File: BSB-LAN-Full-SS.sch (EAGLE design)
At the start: 120 parts, among them IC1 LAN8710A-EZC, IC2 TPS2376DDA, IC3 TX4138, IC4 SY8089AAAC, IC6 CH340X, Q1 BC847, Q2 BC857, Q3 BC847, Q4 WPM2015-3/TR, Q5 BC847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

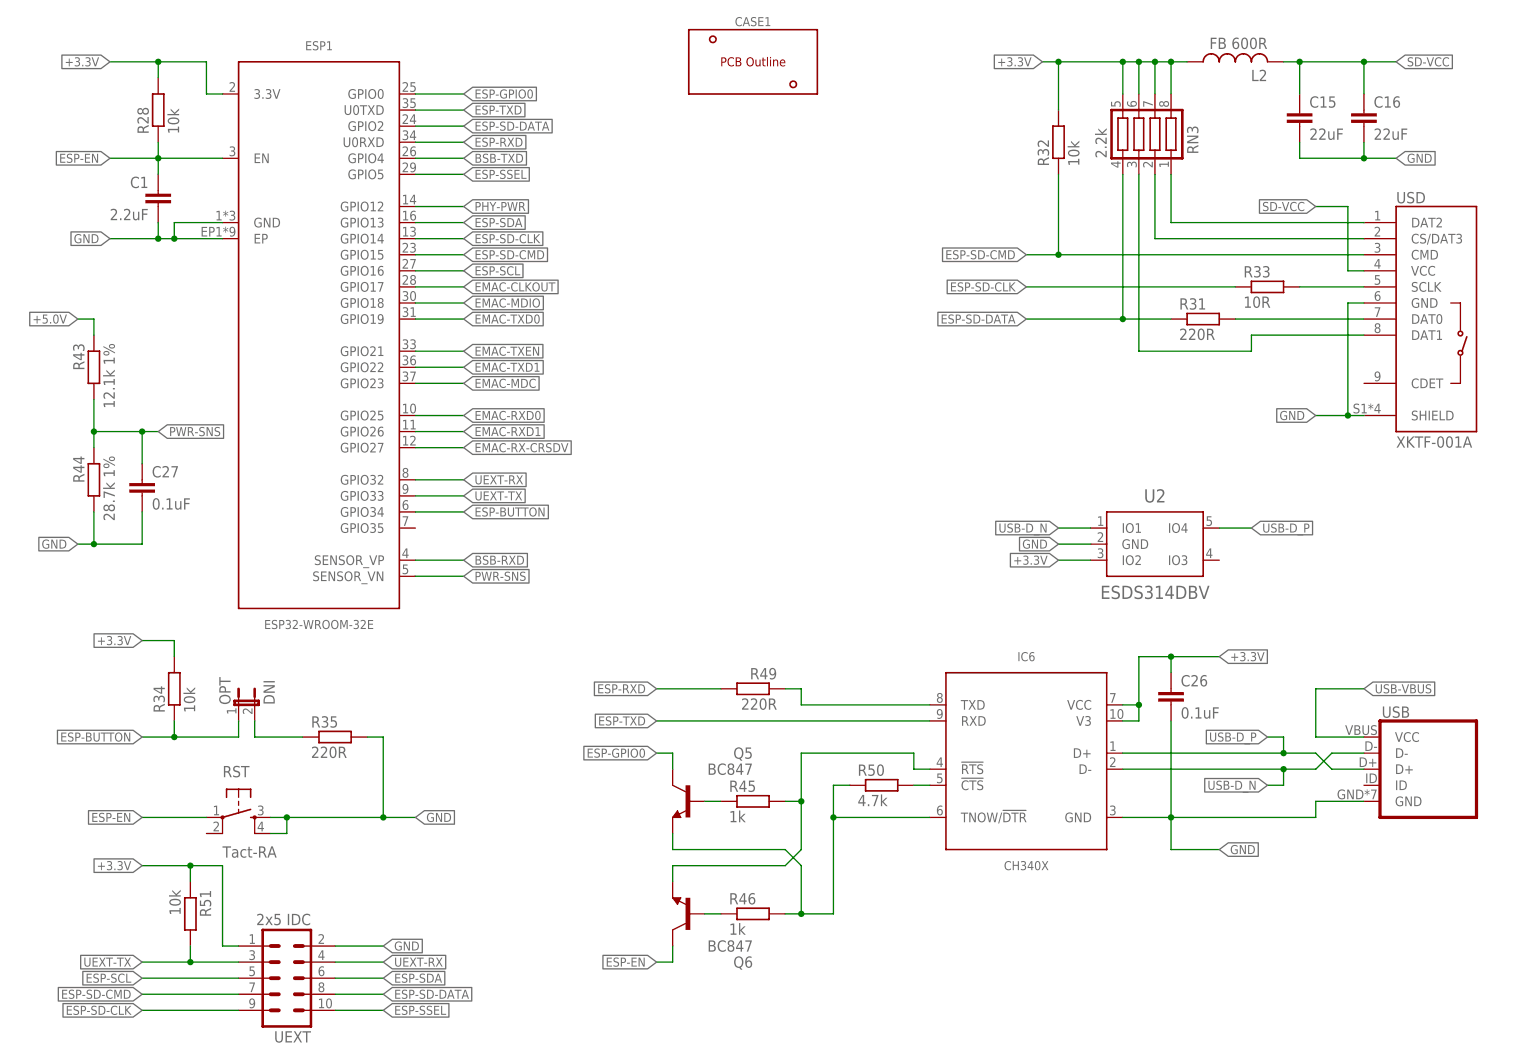
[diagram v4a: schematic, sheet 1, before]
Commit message: Add Missing Pull-Up Resistors on I2C
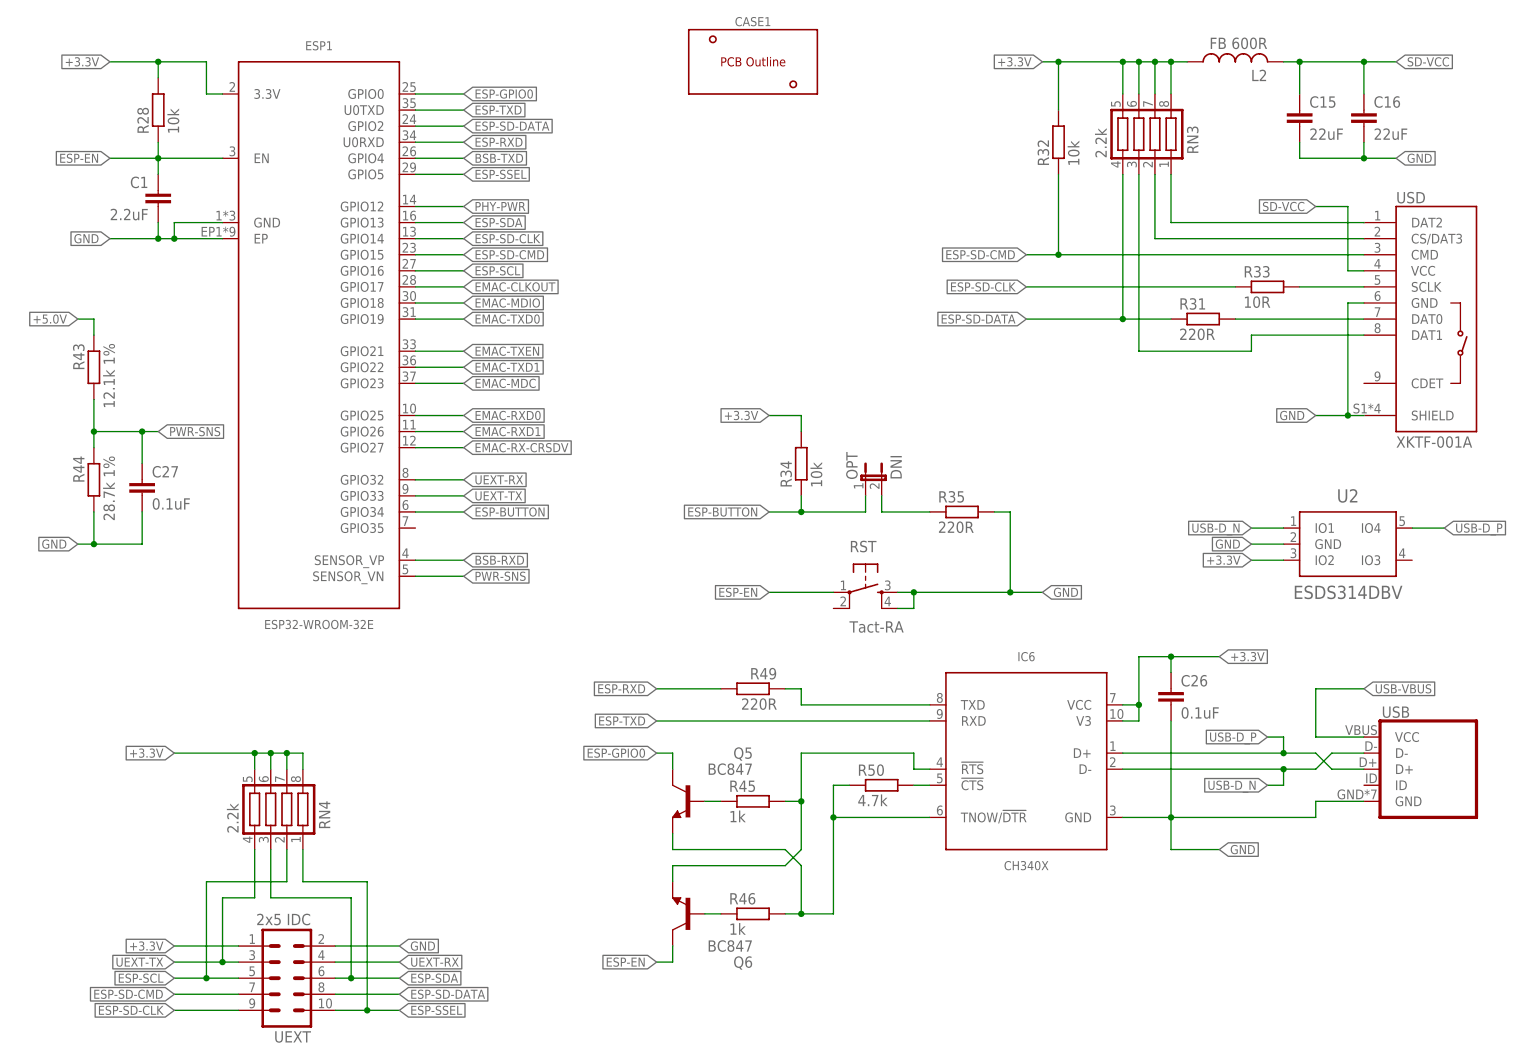
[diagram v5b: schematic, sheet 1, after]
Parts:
- removed R51: 10k, BSB-LAN:R-EU_R0402
- added RN4: 2.2k, BSB-LAN:R-NET-04-R1206
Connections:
- net +3.3V: now also RN4.5, RN4.6, RN4.7, RN4.8; no longer R51.1
- net ESP-SCL: now also RN4.2
- net ESP-SDA: now also RN4.3
- net ESP-SSEL: now also RN4.1
- net UEXT-TX: now also RN4.4; no longer R51.2
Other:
- moved on the sheet: OPT, R34, R35, RST, U2

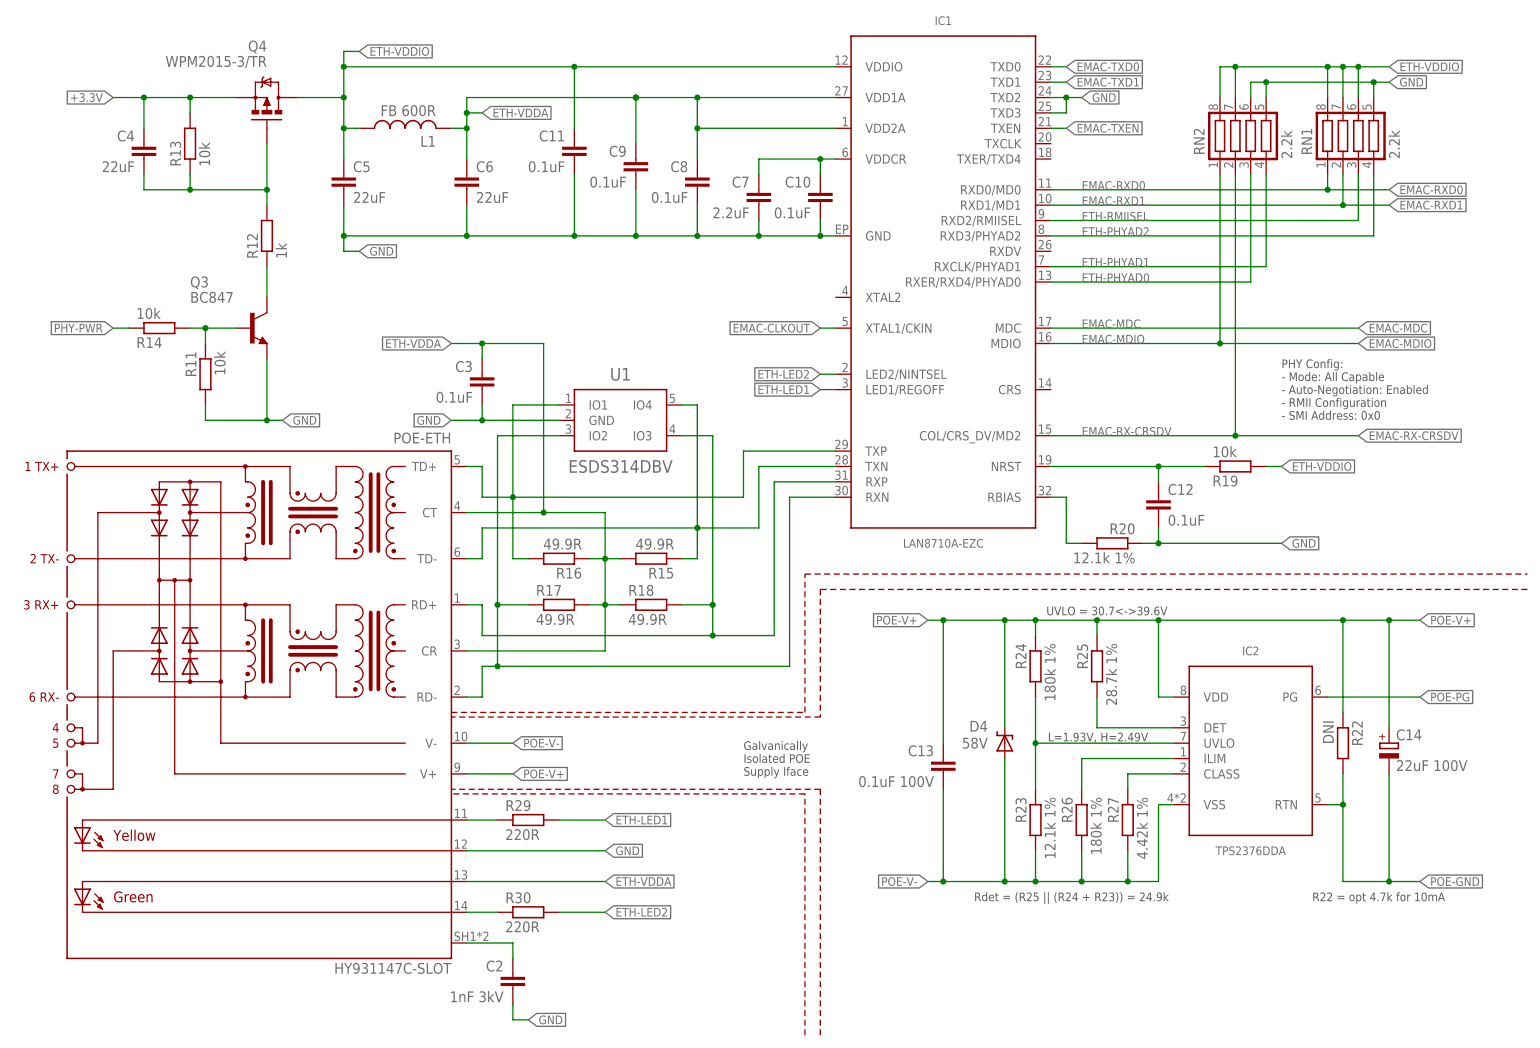
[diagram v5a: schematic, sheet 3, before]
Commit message: Correct Pinout of DC-DC Converter
Not sure quite how I messed up the pin assignments that badly!
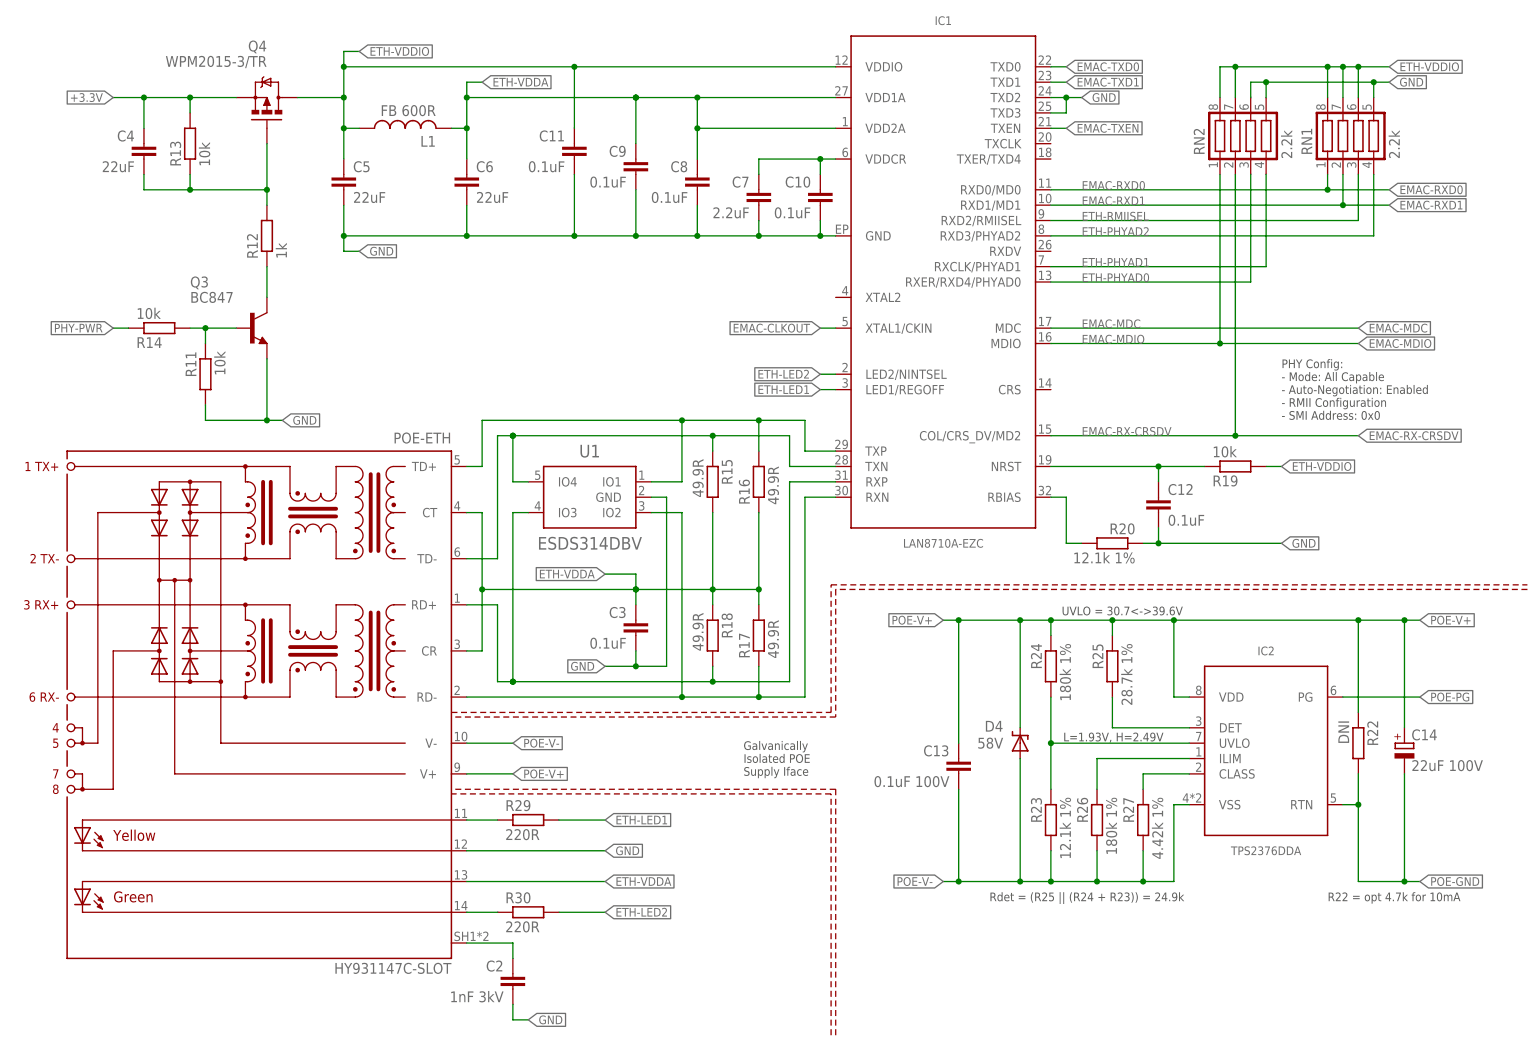
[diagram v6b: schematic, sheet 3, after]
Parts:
- R43: value 12.1k 1% -> 180k 1%
- R44: value 28.7k 1% -> 330k; device BSB-LAN:R-EU_R0402 -> BSB-LAN:R-EU_R0603L
- RST: value Tact-RA -> Tact 19mm
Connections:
- removed net POE-DC-POK-NC: IC3.POK
- net UEXT-RX: now also RN4.4
- net UEXT-TX: no longer RN4.4
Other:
- moved on the sheet: C13, C14, C3, D4, IC2, R15, R16, R17, R18, R22, R23, R24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

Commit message: Correct LCSC_PART Attributes
The power sense divider values were changed, but the attributes didn't get updated.
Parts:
- R43: LCSC_PART C25852 -> C25760
- R44: LCSC_PART C26972 -> C23137
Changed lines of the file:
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@@
 <grid distance="0.1" unitdist="inch" unit="inch" style="lines" multiple="1" display="no" altdistance="0.01" altunitdist="inch" altunit="inch"/>
 <layers>
-<layer number="1" name="Top" color="4" fill="1" visible="yes" active="no"/>
-<layer number="2" name="Route2" color="1" fill="3" visible="yes" active="no"/>
-<layer number="3" name="Route3" color="4" fill="3" visible="yes" active="no"/>
-<layer number="4" name="Route4" color="1" fill="4" visible="yes" active="no"/>
-<layer number="5" name="Route5" color="4" fill="4" visible="yes" active="no"/>
-<layer number="6" name="Route6" color="1" fill="8" visible="yes" active="no"/>
-<layer number="7" name="Route7" color="4" fill="8" visible="yes" active="no"/>
-<layer number="8" name="Route8" color="1" fill="2" visible="yes" active="no"/>
-<layer number="9" name="Route9" color="4" fill="2" visible="yes" active="no"/>
-<layer number="10" name="Route10" color="1" fill="7" visible="yes" active="no"/>
-<layer number="11" name="Route11" color="4" fill="7" visible="yes" active="no"/>
-<layer number="12" name="Route12" color="1" fill="5" visible="yes" active="no"/>
-<layer number="13" name="Route13" color="4" fill="5" visible="yes" active="no"/>
-<layer number="14" name="Route14" color="1" fill="6" visible="yes" active="no"/>
-<layer number="15" name="Route15" color="4" fill="6" visible="yes" active="no"/>
-<layer number="16" name="Bottom" color="1" fill="1" visible="yes" active="no"/>
-<layer number="17" name="Pads" color="2" fill="1" visible="yes" active="no"/>
-<layer number="18" name="Vias" color="2" fill="1" visible="yes" active="no"/>
-<layer number="19" name="Unrouted" color="6" fill="1" visible="yes" active="no"/>
-<layer number="20" name="Dimension" color="15" fill="1" visible="yes" active="no"/>
-<layer number="21" name="tPlace" color="7" fill="1" visible="yes" active="no"/>
-<layer number="22" name="bPlace" color="7" fill="1" visible="yes" active="no"/>
-<layer number="23" name="tOrigins" color="15" fill="1" visible="yes" active="no"/>
-<layer number="24" name="bOrigins" color="15" fill="1" visible="yes" active="no"/>
-<layer number="25" name="tNames" color="7" fill="1" visible="yes" active="no"/>
-<layer number="26" name="bNames" color="7" fill="1" visible="yes" active="no"/>
-<layer number="27" name="tValues" color="7" fill="1" visible="yes" active="no"/>
-<layer number="28" name="bValues" color="7" fill="1" visible="yes" active="no"/>
+<layer number="1" name="Top" color="4" fill="1" visible="no" active="no"/>
+<layer number="2" name="Route2" color="1" fill="3" visible="no" active="no"/>
+<layer number="3" name="Route3" color="4" fill="3" visible="no" active="no"/>
+<layer number="4" name="Route4" color="1" fill="4" visible="no" active="no"/>
+<layer number="5" name="Route5" color="4" fill="4" visible="no" active="no"/>
+<layer number="6" name="Route6" color="1" fill="8" visible="no" active="no"/>
+<layer number="7" name="Route7" color="4" fill="8" visible="no" active="no"/>
+<layer number="8" name="Route8" color="1" fill="2" visible="no" active="no"/>
+<layer number="9" name="Route9" color="4" fill="2" visible="no" active="no"/>
+<layer number="10" name="Route10" color="1" fill="7" visible="no" active="no"/>
+<layer number="11" name="Route11" color="4" fill="7" visible="no" active="no"/>
+<layer number="12" name="Route12" color="1" fill="5" visible="no" active="no"/>
+<layer number="13" name="Route13" color="4" fill="5" visible="no" active="no"/>
+<layer number="14" name="Route14" color="1" fill="6" visible="no" active="no"/>
+<layer number="15" name="Route15" color="4" fill="6" visible="no" active="no"/>
+<layer number="16" name="Bottom" color="1" fill="1" visible="no" active="no"/>
+<layer number="17" name="Pads" color="2" fill="1" visible="no" active="no"/>
+<layer number="18" name="Vias" color="2" fill="1" visible="no" active="no"/>
+<layer number="19" name="Unrouted" color="6" fill="1" visible="no" active="no"/>
+<layer number="20" name="Dimension" color="15" fill="1" visible="no" active="no"/>
+<layer number="21" name="tPlace" color="7" fill="1" visible="no" active="no"/>
+<layer number="22" name="bPlace" color="7" fill="1" visible="no" active="no"/>
+<layer number="23" name="tOrigins" color="15" fill="1" visible="no" active="no"/>
+<layer number="24" name="bOrigins" color="15" fill="1" visible="no" active="no"/>
+<layer number="25" name="tNames" color="7" fill="1" visible="no" active="no"/>
+<layer number="26" name="bNames" color="7" fill="1" visible="no" active="no"/>
+<layer number="27" name="tValues" color="7" fill="1" visible="no" active="no"/>
+<layer number="28" name="bValues" color="7" fill="1" visible="no" active="no"/>
 <layer number="29" name="tStop" color="7" fill="3" visible="no" active="no"/>
 <layer number="30" name="bStop" color="7" fill="6" visible="no" active="no"/>
@@
 <layer number="35" name="tGlue" color="7" fill="4" visible="no" active="no"/>
 <layer number="36" name="bGlue" color="7" fill="5" visible="no" active="no"/>
-<layer number="37" name="tTest" color="7" fill="1" visible="yes" active="no"/>
-<layer number="38" name="bTest" color="7" fill="1" visible="yes" active="no"/>
+<layer number="37" name="tTest" color="7" fill="1" visible="no" active="no"/>
+<layer number="38" name="bTest" color="7" fill="1" visible="no" active="no"/>
 <layer number="39" name="tKeepout" color="4" fill="11" visible="no" active="no"/>
 <layer number="40" name="bKeepout" color="1" fill="11" visible="no" active="no"/>
@@
 <layer number="44" name="Drills" color="7" fill="1" visible="no" active="no"/>
 <layer number="45" name="Holes" color="7" fill="1" visible="no" active="no"/>
-<layer number="46" name="Milling" color="3" fill="1" visible="yes" active="no"/>
-<layer number="47" name="Measures" color="7" fill="1" visible="yes" active="no"/>
-<layer number="48" name="Document" color="7" fill="1" visible="yes" active="no"/>
-<layer number="49" name="Reference" color="7" fill="1" visible="yes" active="no"/>
-<layer number="50" name="dxf" color="7" fill="1" visible="yes" active="no"/>
-<layer number="51" name="tDocu" color="7" fill="1" visible="yes" active="no"/>
-<layer number="52" name="bDocu" color="7" fill="1" visible="yes" active="no"/>
-<layer number="53" name="tGND_GNDA" color="7" fill="9" visible="yes" active="no"/>
-<layer number="54" name="bGND_GNDA" color="1" fill="9" visible="yes" active="no"/>
-<layer number="56" name="wert" color="7" fill="1" visible="yes" active="no"/>
-<layer number="57" name="tCAD" color="7" fill="1" visible="yes" active="no"/>
-<layer number="58" name="bCAD" color="7" fill="1" visible="yes" active="no"/>
-<layer number="59" name="tCarbon" color="7" fill="1" visible="yes" active="no"/>
-<layer number="60" name="bCarbon" color="7" fill="1" visible="yes" active="no"/>
+<layer number="46" name="Milling" color="3" fill="1" visible="no" active="no"/>
+<layer number="47" name="Measures" color="7" fill="1" visible="no" active="no"/>
+<layer number="48" name="Document" color="7" fill="1" visible="no" active="no"/>
+<layer number="49" name="Reference" color="7" fill="1" visible="no" active="no"/>
+<layer number="50" name="dxf" color="7" fill="1" visible="no" active="no"/>
+<layer number="51" name="tDocu" color="7" fill="1" visible="no" active="no"/>
+<layer number="52" name="bDocu" color="7" fill="1" visible="no" active="no"/>
+<layer number="53" name="tGND_GNDA" color="7" fill="9" visible="no" active="no"/>
+<layer number="54" name="bGND_GNDA" color="1" fill="9" visible="no" active="no"/>
+<layer number="56" name="wert" color="7" fill="1" visible="no" active="no"/>
+<layer number="57" name="tCAD" color="7" fill="1" visible="no" active="no"/>
+<layer number="58" name="bCAD" color="7" fill="1" visible="no" active="no"/>
+<layer number="59" name="tCarbon" color="7" fill="1" visible="no" active="no"/>
+<layer number="60" name="bCarbon" color="7" fill="1" visible="no" active="no"/>
 <layer number="88" name="SimResults" color="9" fill="1" visible="yes" active="yes"/>
 <layer number="89" name="SimProbes" color="9" fill="1" visible="yes" active="yes"/>
@@
 </part>
 <part name="R43" library="BSB-LAN" deviceset="R-EU_" device="R0402" value="180k 1%">
-<attribute name="LCSC_PART" value="C25852"/>
+<attribute name="LCSC_PART" value="C25760"/>
 </part>
 <part name="R44" library="BSB-LAN" deviceset="R-EU_" device="R0603L" value="330k">
-<attribute name="LCSC_PART" value="C26972"/>
+<attribute name="LCSC_PART" value="C23137"/>
 </part>
 <part name="C25" library="BSB-LAN" deviceset="C-EU" device="C0805" value="22uF">
